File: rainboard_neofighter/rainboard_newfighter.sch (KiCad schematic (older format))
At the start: 95 parts, among them J1 Conn_01x02, J10 Conn_01x03, J11 SDS-50J, J12 SDS-50J, J13 Conn_01x02, J14 Conn_01x02, J15 Conn_01x02, J16 Conn_01x02, J17 Conn_01x02, J18 Conn_01x02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

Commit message: first draft of v2
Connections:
- wire segments 310 -> 307
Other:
- moved on the sheet: C1, C2, C3, C4, J1, J10, J11, J12, J13, J14, J15, J16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

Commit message: use corrent JST-HX connector
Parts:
- J1, J13, J14, J15, J16, J17, J18, J2, J3, J4, J5, J6, J7, J8: footprint Connector_JST:JST_XH_S2B-XH-A-1_1x02_P2.50mm_Horizontal -> Connector_JST:JST_XH_B2B-XH-AM_1x02_P2.50mm_Vertical
- J10, J9: footprint Connector_JST:JST_XH_S3B-XH-A-1_1x03_P2.50mm_Horizontal -> Connector_JST:JST_XH_B3B-XH-AM_1x03_P2.50mm_Vertical
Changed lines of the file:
@@
 F 0 "J1" H 1580 10787 50  0000 L CNN
 F 1 "Conn_01x02" H 1580 10696 50  0000 L CNN
-F 2 "Connector_JST:JST_XH_S2B-XH-A-1_1x02_P2.50mm_Horizontal" H 1580 10605 50  0001 L CNN
+F 2 "Connector_JST:JST_XH_B2B-XH-AM_1x02_P2.50mm_Vertical" H 1580 10605 50  0001 L CNN
 F 3 "~" H 1500 10750 50  0001 C CNN
 	1    1500 10750
@@
 F 0 "J5" H 1580 12492 50  0000 L CNN
 F 1 "Conn_01x02" H 1580 12401 50  0000 L CNN
-F 2 "Connector_JST:JST_XH_S2B-XH-A-1_1x02_P2.50mm_Horizontal" H 1500 12500 50  0001 C CNN
+F 2 "Connector_JST:JST_XH_B2B-XH-AM_1x02_P2.50mm_Vertical" H 1500 12500 50  0001 C CNN
 F 3 "~" H 1500 12500 50  0001 C CNN
 	1    1500 12500
@@
 F 0 "J6" H 1580 12842 50  0000 L CNN
 F 1 "Conn_01x02" H 1580 12751 50  0000 L CNN
-F 2 "Connector_JST:JST_XH_S2B-XH-A-1_1x02_P2.50mm_Horizontal" H 1500 12850 50  0001 C CNN
+F 2 "Connector_JST:JST_XH_B2B-XH-AM_1x02_P2.50mm_Vertical" H 1500 12850 50  0001 C CNN
 F 3 "~" H 1500 12850 50  0001 C CNN
 	1    1500 12850
@@
 F 0 "J7" H 1580 13242 50  0000 L CNN
 F 1 "Conn_01x02" H 1580 13151 50  0000 L CNN
-F 2 "Connector_JST:JST_XH_S2B-XH-A-1_1x02_P2.50mm_Horizontal" H 1500 13250 50  0001 C CNN
+F 2 "Connector_JST:JST_XH_B2B-XH-AM_1x02_P2.50mm_Vertical" H 1500 13250 50  0001 C CNN
 F 3 "~" H 1500 13250 50  0001 C CNN
 	1    1500 13250
@@
 F 0 "J8" H 1580 13592 50  0000 L CNN
 F 1 "Conn_01x02" H 1580 13501 50  0000 L CNN
-F 2 "Connector_JST:JST_XH_S2B-XH-A-1_1x02_P2.50mm_Horizontal" H 1500 13600 50  0001 C CNN
+F 2 "Connector_JST:JST_XH_B2B-XH-AM_1x02_P2.50mm_Vertical" H 1500 13600 50  0001 C CNN
 F 3 "~" H 1500 13600 50  0001 C CNN
 	1    1500 13600
@@
 F 0 "J9" V 9877 11880 50  0000 L CNN
 F 1 "Conn_01x03" V 9968 11880 50  0000 L CNN
-F 2 "Connector_JST:JST_XH_S3B-XH-A-1_1x03_P2.50mm_Horizontal" V 10059 11880 50  0001 L CNN
+F 2 "Connector_JST:JST_XH_B3B-XH-AM_1x03_P2.50mm_Vertical" V 10059 11880 50  0001 L CNN
 F 3 "~" H 10050 11700 50  0001 C CNN
 	1    10050 11700
@@
 F 0 "J10" V 10177 12780 50  0000 L CNN
 F 1 "Conn_01x03" V 10268 12780 50  0000 L CNN
-F 2 "Connector_JST:JST_XH_S3B-XH-A-1_1x03_P2.50mm_Horizontal" V 10359 12780 50  0001 L CNN
+F 2 "Connector_JST:JST_XH_B3B-XH-AM_1x03_P2.50mm_Vertical" V 10359 12780 50  0001 L CNN
 F 3 "~" H 10350 12600 50  0001 C CNN
 	1    10350 12600
@@
 F 0 "J13" H 5730 10292 50  0000 L CNN
 F 1 "Conn_01x02" H 5730 10201 50  0000 L CNN
-F 2 "Connector_JST:JST_XH_S2B-XH-A-1_1x02_P2.50mm_Horizontal" H 5650 10300 50  0001 C CNN
+F 2 "Connector_JST:JST_XH_B2B-XH-AM_1x02_P2.50mm_Vertical" H 5650 10300 50  0001 C CNN
 F 3 "~" H 5650 10300 50  0001 C CNN
 	1    5650 10300
@@
 F 0 "J14" H 5730 10642 50  0000 L CNN
 F 1 "Conn_01x02" H 5730 10551 50  0000 L CNN
-F 2 "Connector_JST:JST_XH_S2B-XH-A-1_1x02_P2.50mm_Horizontal" H 5650 10650 50  0001 C CNN
+F 2 "Connector_JST:JST_XH_B2B-XH-AM_1x02_P2.50mm_Vertical" H 5650 10650 50  0001 C CNN
 F 3 "~" H 5650 10650 50  0001 C CNN
 	1    5650 10650
@@
 F 0 "J15" H 5730 10992 50  0000 L CNN
 F 1 "Conn_01x02" H 5730 10901 50  0000 L CNN
-F 2 "Connector_JST:JST_XH_S2B-XH-A-1_1x02_P2.50mm_Horizontal" H 5650 11000 50  0001 C CNN
+F 2 "Connector_JST:JST_XH_B2B-XH-AM_1x02_P2.50mm_Vertical" H 5650 11000 50  0001 C CNN
 F 3 "~" H 5650 11000 50  0001 C CNN
 	1    5650 11000
@@
 F 0 "J16" H 5730 11342 50  0000 L CNN
 F 1 "Conn_01x02" H 5730 11251 50  0000 L CNN
-F 2 "Connector_JST:JST_XH_S2B-XH-A-1_1x02_P2.50mm_Horizontal" H 5650 11350 50  0001 C CNN
+F 2 "Connector_JST:JST_XH_B2B-XH-AM_1x02_P2.50mm_Vertical" H 5650 11350 50  0001 C CNN
 F 3 "~" H 5650 11350 50  0001 C CNN
 	1    5650 11350
@@
 F 0 "J4" H 1580 12042 50  0000 L CNN
 F 1 "Conn_01x02" H 1580 11951 50  0000 L CNN
-F 2 "Connector_JST:JST_XH_S2B-XH-A-1_1x02_P2.50mm_Horizontal" H 1500 12050 50  0001 C CNN
+F 2 "Connector_JST:JST_XH_B2B-XH-AM_1x02_P2.50mm_Vertical" H 1500 12050 50  0001 C CNN
 F 3 "~" H 1500 12050 50  0001 C CNN
 	1    1500 12050
@@
 F 0 "J3" H 1580 11592 50  0000 L CNN
 F 1 "Conn_01x02" H 1580 11501 50  0000 L CNN
-F 2 "Connector_JST:JST_XH_S2B-XH-A-1_1x02_P2.50mm_Horizontal" H 1500 11600 50  0001 C CNN
+F 2 "Connector_JST:JST_XH_B2B-XH-AM_1x02_P2.50mm_Vertical" H 1500 11600 50  0001 C CNN
 F 3 "~" H 1500 11600 50  0001 C CNN
 	1    1500 11600
@@
 F 0 "J2" H 1580 11142 50  0000 L CNN
 F 1 "Conn_01x02" H 1580 11051 50  0000 L CNN
-F 2 "Connector_JST:JST_XH_S2B-XH-A-1_1x02_P2.50mm_Horizontal" H 1500 11150 50  0001 C CNN
+F 2 "Connector_JST:JST_XH_B2B-XH-AM_1x02_P2.50mm_Vertical" H 1500 11150 50  0001 C CNN
 F 3 "~" H 1500 11150 50  0001 C CNN
 	1    1500 11150
@@
 F 0 "J17" H 5730 11692 50  0000 L CNN
 F 1 "Conn_01x02" H 5730 11601 50  0000 L CNN
-F 2 "Connector_JST:JST_XH_S2B-XH-A-1_1x02_P2.50mm_Horizontal" H 5650 11700 50  0001 C CNN
+F 2 "Connector_JST:JST_XH_B2B-XH-AM_1x02_P2.50mm_Vertical" H 5650 11700 50  0001 C CNN
 F 3 "~" H 5650 11700 50  0001 C CNN
 	1    5650 11700
@@
 F 0 "J18" H 5730 12042 50  0000 L CNN
 F 1 "Conn_01x02" H 5730 11951 50  0000 L CNN
-F 2 "Connector_JST:JST_XH_S2B-XH-A-1_1x02_P2.50mm_Horizontal" H 5650 12050 50  0001 C CNN
+F 2 "Connector_JST:JST_XH_B2B-XH-AM_1x02_P2.50mm_Vertical" H 5650 12050 50  0001 C CNN
 F 3 "~" H 5650 12050 50  0001 C CNN
 	1    5650 12050

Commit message: move decoupling caps close to ICs
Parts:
- C1, C2, C3, C4: LCSC (none) -> C28323
- U1: LCSC (none) -> C47023
- U3: LCSC (none) -> C142286
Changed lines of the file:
@@
 F 2 "Capacitor_SMD:C_0603_1608Metric" H 2238 9600 50  0001 C CNN
 F 3 "~" H 2200 9750 50  0001 C CNN
+F 4 "C28323" H 2200 9750 50  0001 C CNN "LCSC"
 	1    2200 9750
 	1    0    0    -1
@@
 F 2 "Capacitor_SMD:C_0603_1608Metric" H 8238 11000 50  0001 C CNN
 F 3 "~" H 8200 11150 50  0001 C CNN
+F 4 "C28323" H 8200 11150 50  0001 C CNN "LCSC"
 	1    8200 11150
 	1    0    0    -1
@@
 F 2 "Capacitor_SMD:C_0603_1608Metric" H 12788 11750 50  0001 C CNN
 F 3 "~" H 12750 11900 50  0001 C CNN
+F 4 "C28323" H 12750 11900 50  0001 C CNN "LCSC"
 	1    12750 11900
 	1    0    0    -1
@@
 F 2 "Capacitor_SMD:C_0603_1608Metric" H 20638 12650 50  0001 C CNN
 F 3 "~" H 20600 12800 50  0001 C CNN
+F 4 "C28323" H 20600 12800 50  0001 C CNN "LCSC"
 	1    20600 12800
 	1    0    0    -1
@@
 F 8 "Everlight" H 15050 12000 50  0001 L BNN "Field8"
 F 9 "Optocoupler [Everlight Electronics] EL357N_A__TA_-G Optocoupler" H 15050 12000 50  0001 L BNN "Field9"
+F 10 "C142286" V 15050 12000 50  0001 C CNN "LCSC"
 	1    15050 12000
 	1    0    0    -1
@@
 F 2 "io_expander:SOIC127P1030X265-28N" H 3650 11050 50  0001 L BNN
 F 3 "0.4" H 3650 11050 50  0001 L BNN
-F 4 "" H 3650 11050 50  0001 L BNN "Field4"
+F 4 "C47023" H 3650 11050 50  0001 L BNN "LCSC"
 F 5 "" H 3650 11050 50  0001 L BNN "Field5"
 F 6 "1.27" H 3650 11050 50  0001 L BNN "Field6"

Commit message: Add LCSC JLCPCB part data for each component
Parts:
- C1, C2, C3, C4: value 0.1uf -> 100nf; LCSC C28323 -> C14663
- R1, R2: LCSC (none) -> C25803
- R3, R4: LCSC (none) -> C23162
- R5, R6, R7: LCSC (none) -> C4190
- R8: LCSC (none) -> C25804
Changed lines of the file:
@@
 F 2 "Resistor_SMD:R_0603_1608Metric" V 9330 10850 50  0001 C CNN
 F 3 "~" H 9400 10850 50  0001 C CNN
+F 4 "C23162" H 9400 10850 50  0001 C CNN "LCSC"
 	1    9400 10850
 	1    0    0    -1
@@
 F 2 "Resistor_SMD:R_0603_1608Metric" V 9330 12900 50  0001 C CNN
 F 3 "~" H 9400 12900 50  0001 C CNN
+F 4 "C23162" H 9400 12900 50  0001 C CNN "LCSC"
 	1    9400 12900
-	1    0    0    -1
-$EndComp
-$Comp
-L Device:C C1
-U 1 1 5F7A5732
-P 2200 9750
-F 0 "C1" H 2315 9796 50  0000 L CNN
-F 1 "0.1uf" H 2315 9705 50  0000 L CNN
-F 2 "Capacitor_SMD:C_0603_1608Metric" H 2238 9600 50  0001 C CNN
-F 3 "~" H 2200 9750 50  0001 C CNN
-F 4 "C28323" H 2200 9750 50  0001 C CNN "LCSC"
-	1    2200 9750
 	1    0    0    -1
 $EndComp
@@
 F 2 "Resistor_SMD:R_0603_1608Metric" V 8430 12100 50  0001 C CNN
 F 3 "~" H 8500 12100 50  0001 C CNN
+F 4 "C25803" H 8500 12100 50  0001 C CNN "LCSC"
 	1    8500 12100
 	1    0    0    -1
@@
 P 8200 11150
 F 0 "C2" H 8315 11196 50  0000 L CNN
-F 1 "0.1uf" H 8315 11105 50  0000 L CNN
+F 1 "100nf" H 8315 11105 50  0000 L CNN
 F 2 "Capacitor_SMD:C_0603_1608Metric" H 8238 11000 50  0001 C CNN
 F 3 "~" H 8200 11150 50  0001 C CNN
-F 4 "C28323" H 8200 11150 50  0001 C CNN "LCSC"
+F 4 "C14663" H 8200 11150 50  0001 C CNN "LCSC"
 	1    8200 11150
 	1    0    0    -1
@@
 F 2 "Resistor_SMD:R_0603_1608Metric" V 20030 11200 50  0001 C CNN
 F 3 "~" H 20100 11200 50  0001 C CNN
+F 4 "C4190" H 20100 11200 50  0001 C CNN "LCSC"
 	1    20100 11200
 	1    0    0    -1
@@
 F 2 "Resistor_SMD:R_0603_1608Metric" V 20080 12200 50  0001 C CNN
 F 3 "~" H 20150 12200 50  0001 C CNN
+F 4 "C4190" H 20150 12200 50  0001 C CNN "LCSC"
 	1    20150 12200
 	1    0    0    -1
@@
 F 2 "Resistor_SMD:R_0603_1608Metric" V 8930 12900 50  0001 C CNN
 F 3 "~" H 9000 12900 50  0001 C CNN
+F 4 "C25803" H 9000 12900 50  0001 C CNN "LCSC"
 	1    9000 12900
 	1    0    0    -1
@@
 P 12750 11900
 F 0 "C4" H 12865 11946 50  0000 L CNN
-F 1 "0.1uf" H 12865 11855 50  0000 L CNN
+F 1 "100nf" H 12865 11855 50  0000 L CNN
 F 2 "Capacitor_SMD:C_0603_1608Metric" H 12788 11750 50  0001 C CNN
 F 3 "~" H 12750 11900 50  0001 C CNN
-F 4 "C28323" H 12750 11900 50  0001 C CNN "LCSC"
+F 4 "C14663" H 12750 11900 50  0001 C CNN "LCSC"
 	1    12750 11900
 	1    0    0    -1
@@
 P 20600 12800
 F 0 "C3" H 20715 12846 50  0000 L CNN
-F 1 "0.1uf" H 20715 12755 50  0000 L CNN
+F 1 "100nf" H 20715 12755 50  0000 L CNN
 F 2 "Capacitor_SMD:C_0603_1608Metric" H 20638 12650 50  0001 C CNN
 F 3 "~" H 20600 12800 50  0001 C CNN
-F 4 "C28323" H 20600 12800 50  0001 C CNN "LCSC"
+F 4 "C14663" H 20600 12800 50  0001 C CNN "LCSC"
 	1    20600 12800
 	1    0    0    -1
@@
 F 2 "Resistor_SMD:R_0603_1608Metric" V 14330 11900 50  0001 C CNN
 F 3 "~" H 14400 11900 50  0001 C CNN
+F 4 "C4190" H 14400 11900 50  0001 C CNN "LCSC"
 	1    14400 11900
 	0    -1   -1   0
@@
 U 1 1 61396682
 P 15750 11550
-F 0 "R8" H 15820 11596 50  0000 L CNN
-F 1 "10k" H 15820 11505 50  0000 L CNN
+F 0 "R8" H 15680 11504 50  0000 R CNN
+F 1 "10k" H 15680 11595 50  0000 R CNN
 F 2 "Resistor_SMD:R_0603_1608Metric" V 15680 11550 50  0001 C CNN
 F 3 "~" H 15750 11550 50  0001 C CNN
+F 4 "C25804" H 15750 11550 50  0001 C CNN "LCSC"
 	1    15750 11550
 	-1   0    0    1
@@
 Text GLabel 1250 1250 0    50   Input ~ 0
 MIDI-IN
+$Comp
+L Device:C C1
+U 1 1 5F7A5732
+P 2200 9750
+F 0 "C1" H 2315 9796 50  0000 L CNN
+F 1 "100nf" H 2315 9705 50  0000 L CNN
+F 2 "Capacitor_SMD:C_0603_1608Metric" H 2238 9600 50  0001 C CNN
+F 3 "~" H 2200 9750 50  0001 C CNN
+F 4 "C14663" H 2200 9750 50  0001 C CNN "LCSC"
+	1    2200 9750
+	1    0    0    -1
+$EndComp
 $EndSCHEMATC

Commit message: Add LCSC JLCPCB part data for each component
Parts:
- U2: LCSC (none) -> C5605
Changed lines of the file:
@@
 F 6 "NXP" H 19250 12550 50  0001 L BNN "Field6"
 F 7 "SOIC-14" H 19250 12550 50  0001 L BNN "Field7"
+F 8 "C5605" H 19250 12550 50  0001 C CNN "LCSC"
 	1    19250 12550
 	1    0    0    -1
@@
 F 43 "" H 3650 11050 50  0001 L BNN "Field43"
 F 44 "10.3" H 3650 11050 50  0001 L BNN "Field44"
+F 45 "C47023" H 3650 11050 50  0001 C CNN "LCSC"
 	1    3650 11050
 	1    0    0    -1

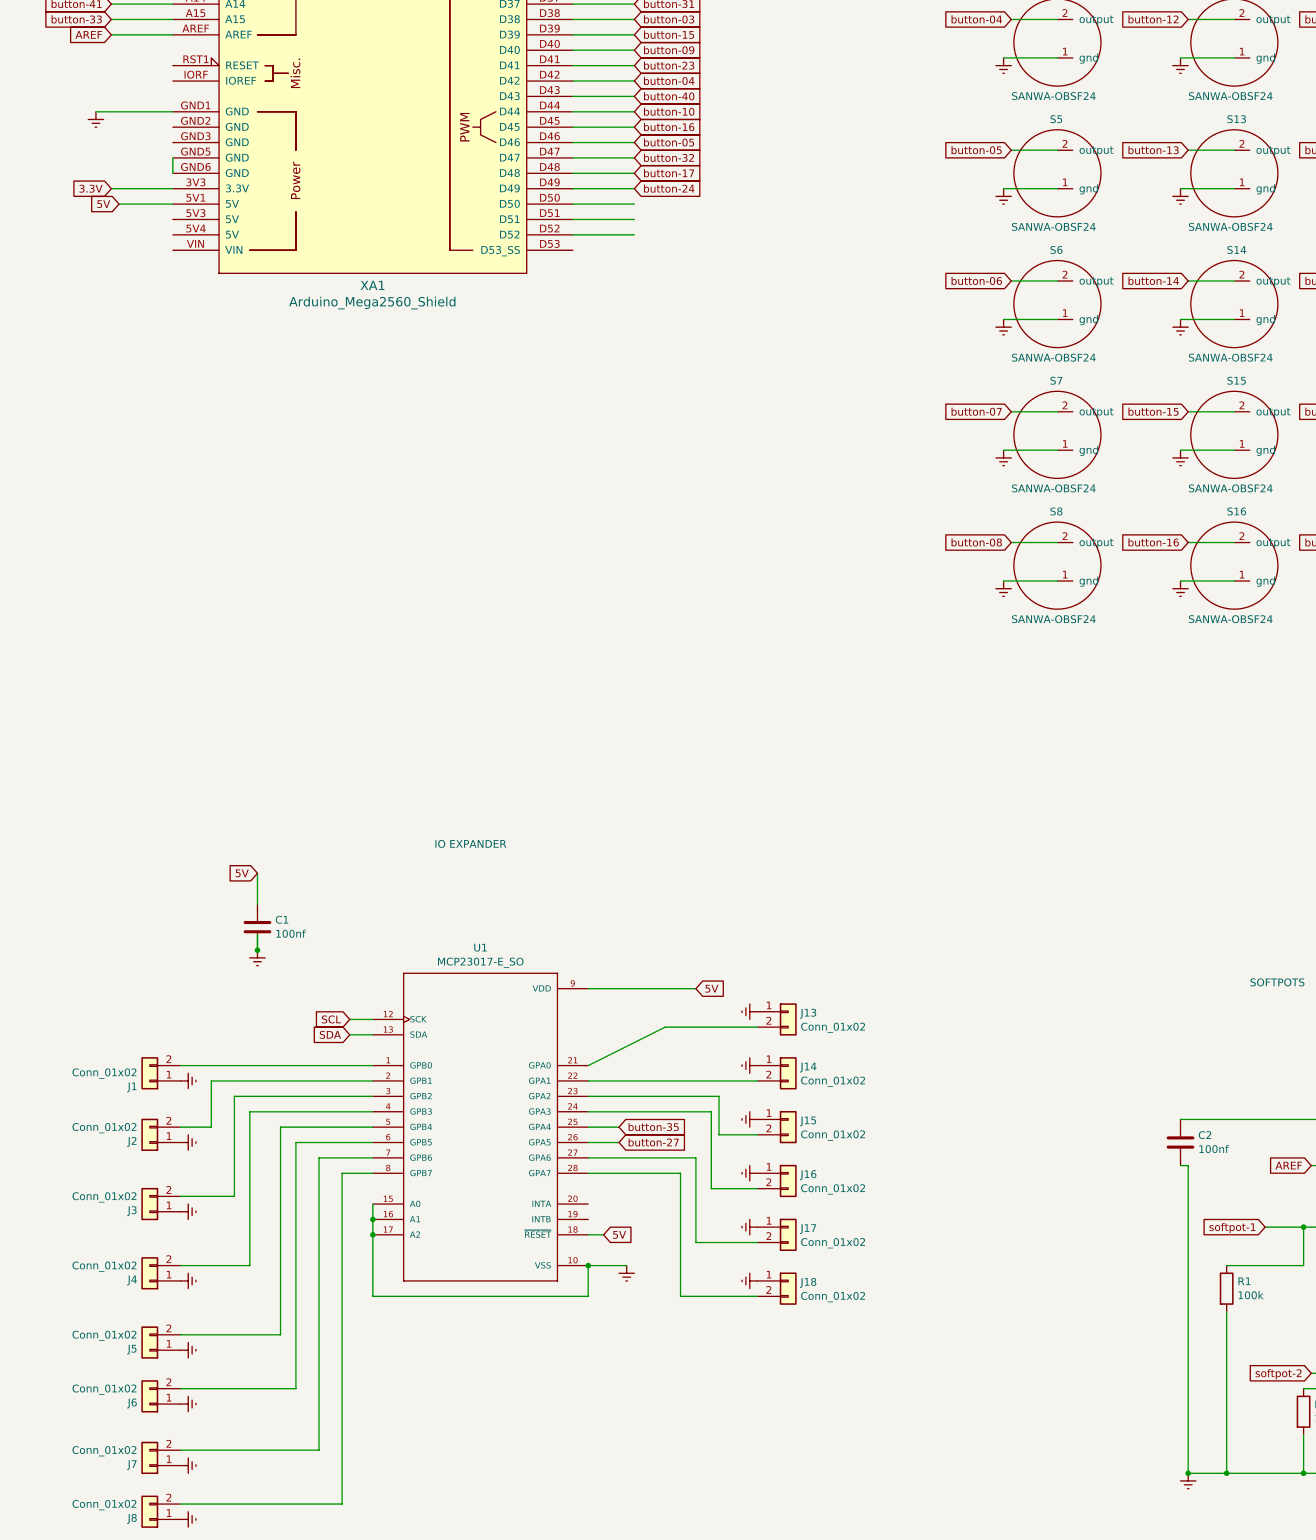
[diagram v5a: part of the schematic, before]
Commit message: Create analog ground network
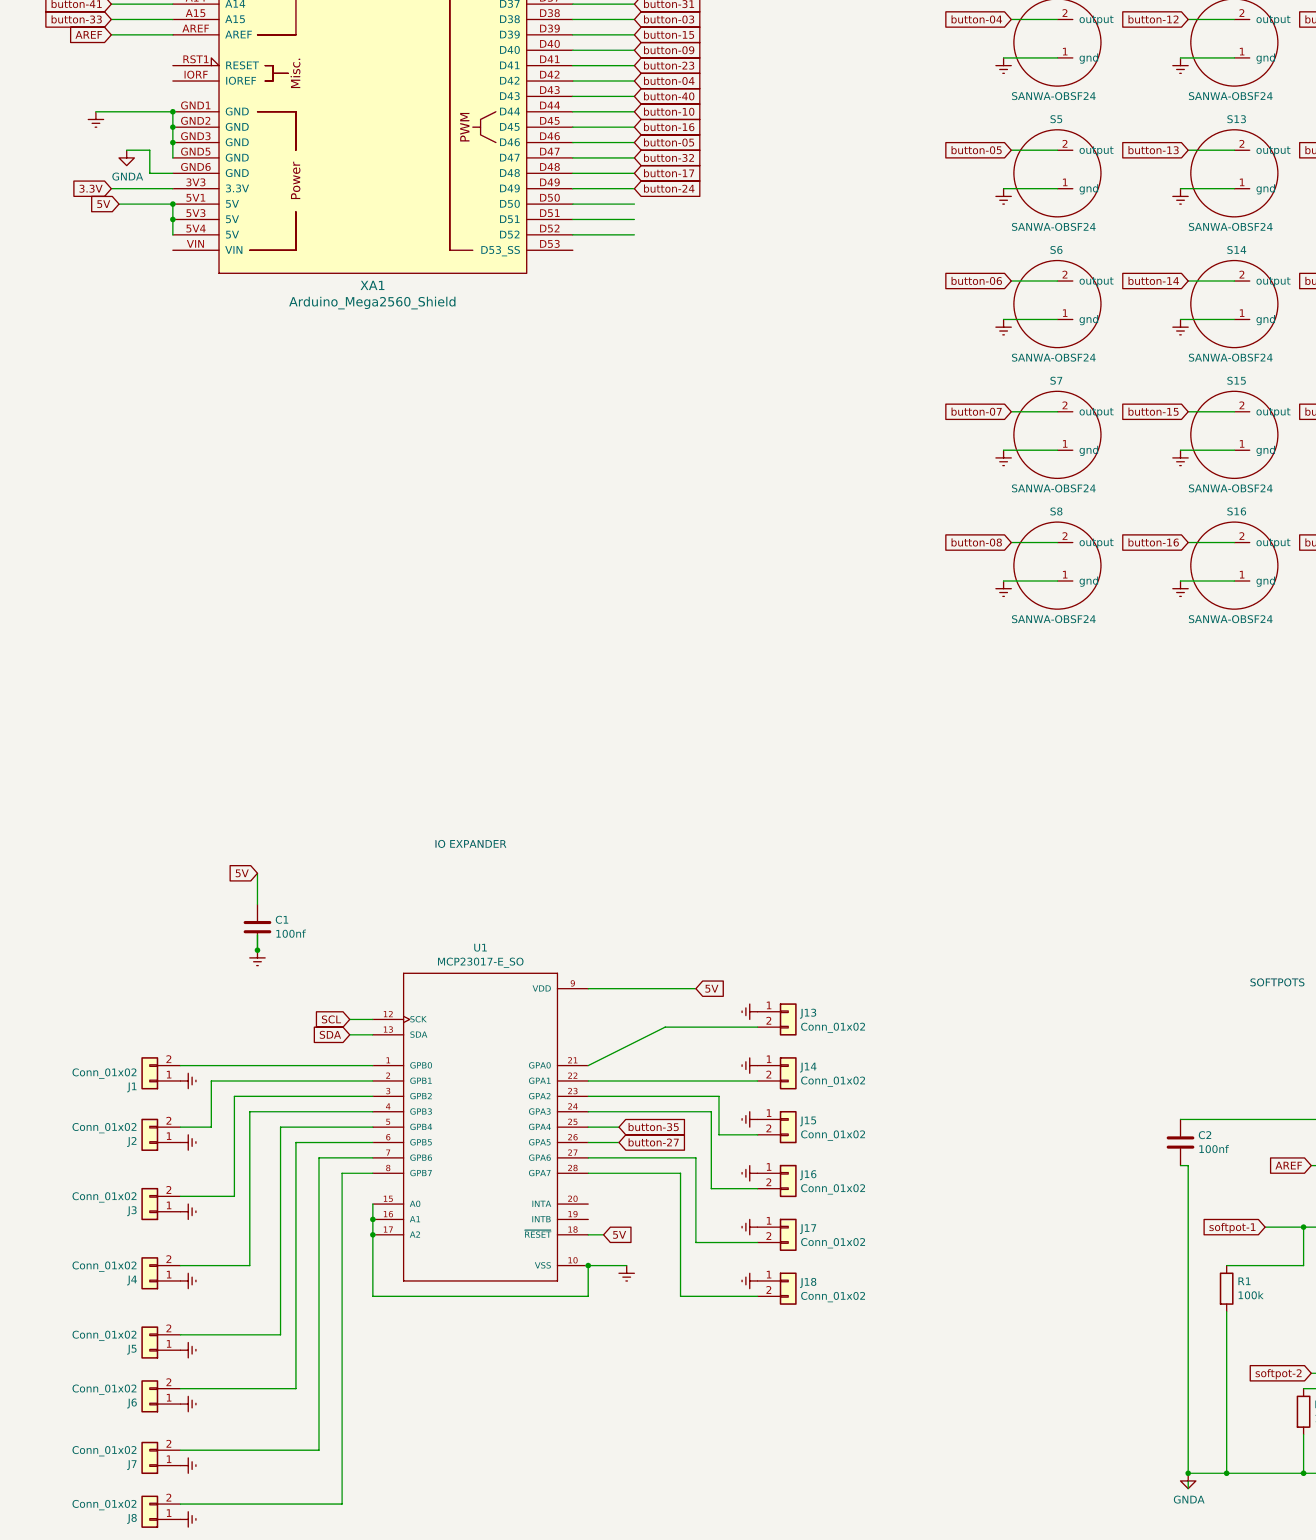
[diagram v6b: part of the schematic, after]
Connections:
- net 5V: now also XA1.5V3 (5V), XA1.5V4 (5V)
- net Earth: now also XA1.GND2 (GND), XA1.GND3 (GND), XA1.GND5 (GND); no longer C2.2, R1.2, R2.2, R4.2
- net GNDA: now reaches XA1.GND6 (GND)
- net GNDA: now also C2.2, R1.2, R2.2, R4.2; no longer XA1.GND5 (GND)
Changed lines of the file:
@@
 Wire Wire Line
 	14300 7250 14000 7250
-Wire Wire Line
-	1150 4450 1650 4450
 Text GLabel 1250 1650 0    50   Input ~ 0
 button-46
@@
 Text GLabel 1300 5050 0    50   Input ~ 0
 5V
-Wire Wire Line
-	1300 5050 1650 5050
 Text GLabel 1050 3250 0    50   Input ~ 0
 softpot-1
@@
 	1    0    0    -1
 $EndComp
-Wire Wire Line
-	1650 4750 1650 4850
 $Comp
 L power:Earth #PWR0102
@@
 Wire Wire Line
 	8200 11000 9400 11000
-$Comp
-L power:Earth #PWR0104
-U 1 1 5FA22592
-P 8250 13300
-F 0 "#PWR0104" H 8250 13050 50  0001 C CNN
-F 1 "Earth" H 8250 13150 50  0001 C CNN
-F 2 "" H 8250 13300 50  0001 C CNN
-F 3 "~" H 8250 13300 50  0001 C CNN
-	1    8250 13300
-	1    0    0    -1
-$EndComp
 Wire Wire Line
 	8250 13300 8250 11300
@@
 	9400 12500 9400 11600
 Connection ~ 9400 11600
-Connection ~ 8250 13300
 Wire Wire Line
 	9400 13050 9400 13300
@@
 	1    0    0    -1
 $EndComp
+$Comp
+L power:GNDA #PWR0124
+U 1 1 63D6B335
+P 8250 13300
+F 0 "#PWR0124" H 8250 13050 50  0001 C CNN
+F 1 "GNDA" H 8255 13127 50  0000 C CNN
+F 2 "" H 8250 13300 50  0001 C CNN
+F 3 "" H 8250 13300 50  0001 C CNN
+	1    8250 13300
+	1    0    0    -1
+$EndComp
+Connection ~ 8250 13300
+Wire Wire Line
+	8250 13400 8250 13350
+Wire Wire Line
+	1300 5050 1650 5050
+Wire Wire Line
+	1650 5250 1650 5150
+Connection ~ 1650 5050
+Connection ~ 1650 5150
+Wire Wire Line
+	1650 5150 1650 5050
+Wire Wire Line
+	1150 4450 1650 4450
+$Comp
+L power:GNDA #PWR0104
+U 1 1 63CEC50B
+P 1350 4700
+F 0 "#PWR0104" H 1350 4450 50  0001 C CNN
+F 1 "GNDA" H 1355 4527 50  0000 C CNN
+F 2 "" H 1350 4700 50  0001 C CNN
+F 3 "" H 1350 4700 50  0001 C CNN
+	1    1350 4700
+	1    0    0    -1
+$EndComp
+Wire Wire Line
+	1350 4700 1500 4700
+Wire Wire Line
+	1500 4700 1500 4850
+Wire Wire Line
+	1500 4850 1650 4850
+Wire Wire Line
+	1650 4450 1650 4550
+Connection ~ 1650 4450
+Connection ~ 1650 4550
+Wire Wire Line
+	1650 4550 1650 4650
+Connection ~ 1650 4650
+Wire Wire Line
+	1650 4650 1650 4750
 $EndSCHEMATC
